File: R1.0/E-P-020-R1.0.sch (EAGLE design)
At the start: 42 parts, among them CN1 1X4-CLEANBIG, J1 1445055-3, U2 ATMEGA328P_PDIP

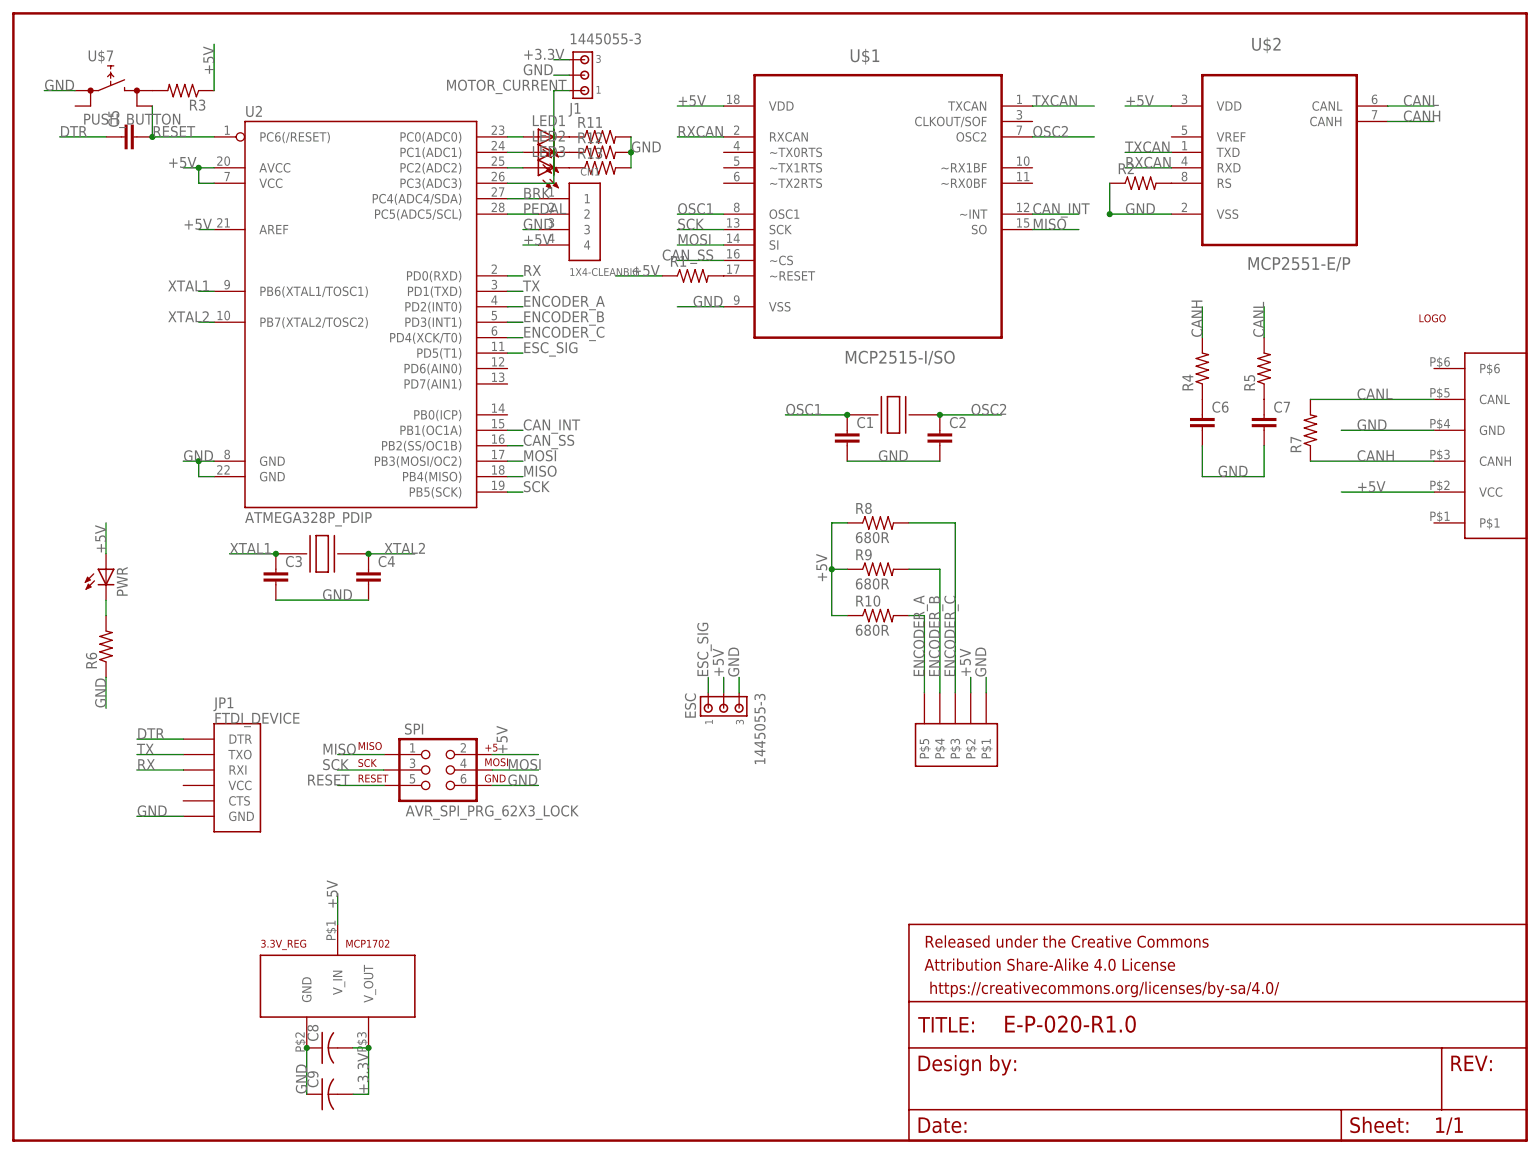
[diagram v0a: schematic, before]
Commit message: Added resistor/capacitor values
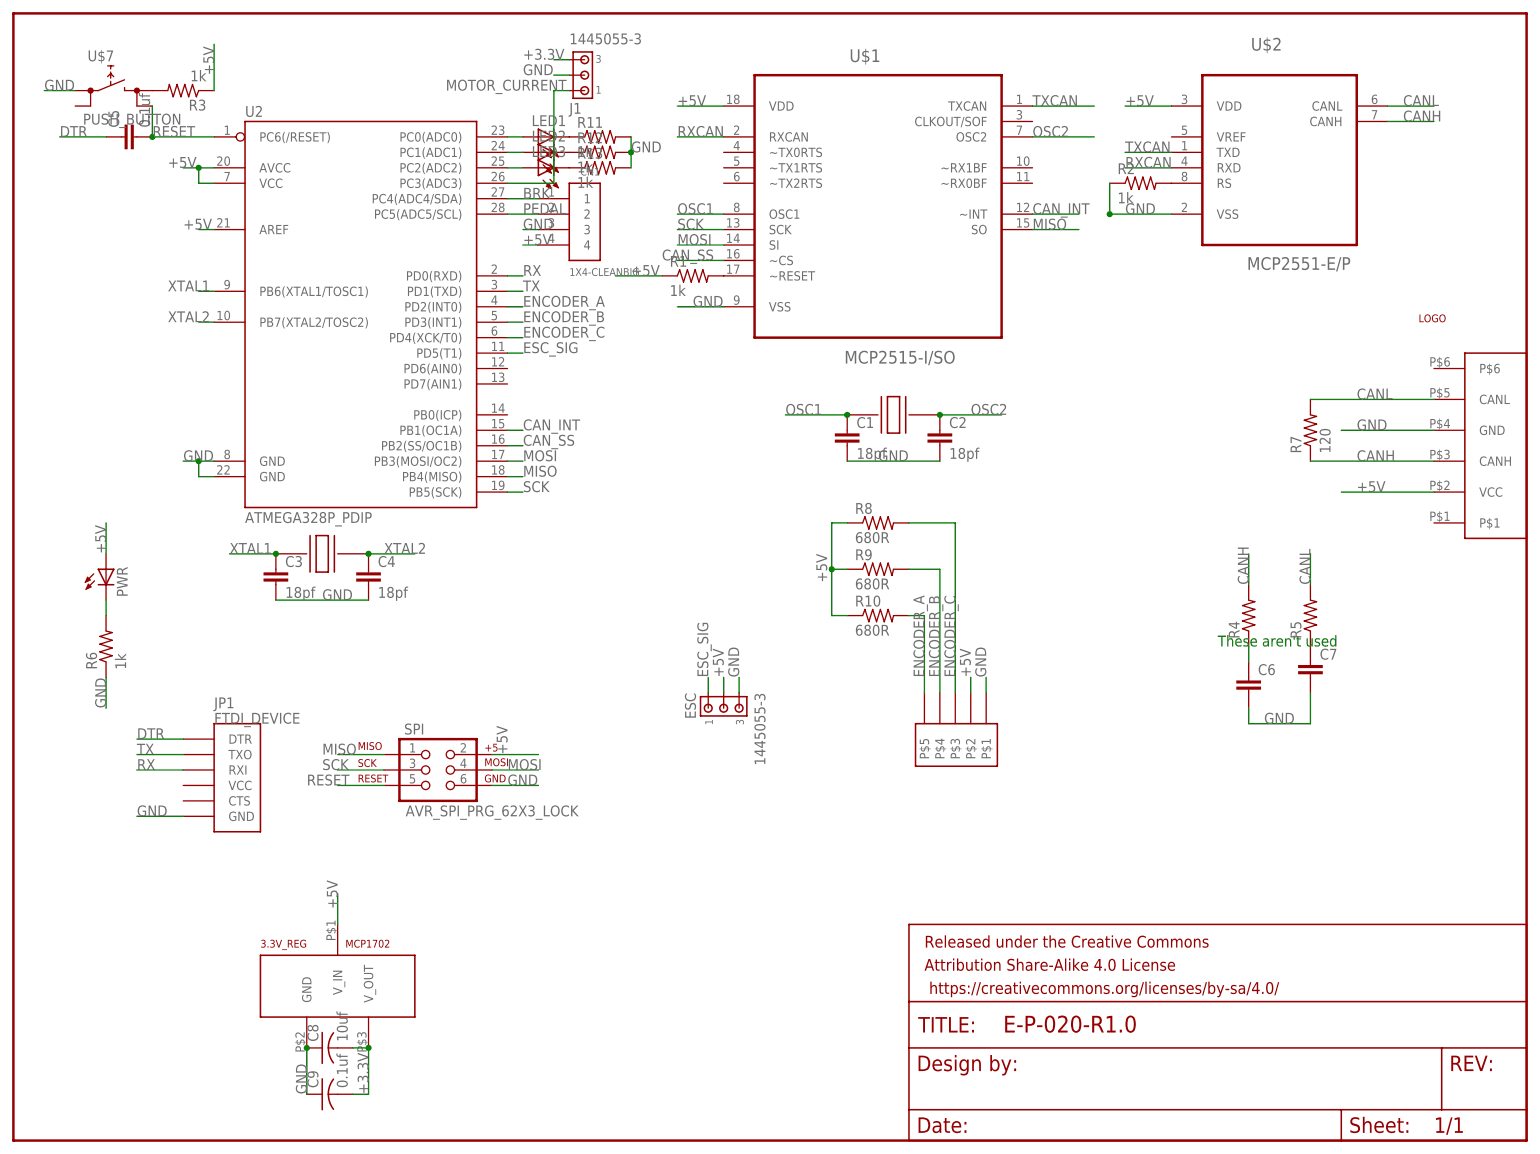
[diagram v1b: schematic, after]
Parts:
- C1, C2, C3, C4: value (none) -> 18pf
- C5, C9: value (none) -> 0.1uf
- C8: value (none) -> 10uf
- R1, R11, R12, R13, R2, R3, R6: value (none) -> 1k
- R7: value (none) -> 120
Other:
- note added: "These aren't used"
- moved on the sheet: C6, C7, R4, R5
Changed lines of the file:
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@@
 <part name="U$1" library="Microchip_By_element14_Batch_1" deviceset="MCP2515-I/SO" device=""/>
 <part name="U$2" library="Microchip_By_element14_Batch_1" deviceset="MCP2551-E/P" device=""/>
-<part name="R1" library="SparkFun-Passives" deviceset="RESISTOR" device="0805-RES"/>
+<part name="R1" library="SparkFun-Passives" deviceset="RESISTOR" device="0805-RES" value="1k"/>
 <part name="U$3" library="mylibrary" deviceset="CRYSTAL" device=""/>
-<part name="C1" library="SparkFun-Capacitors" deviceset="CAP" device="0805"/>
-<part name="C2" library="SparkFun-Capacitors" deviceset="CAP" device="0805"/>
+<part name="C1" library="SparkFun-Capacitors" deviceset="CAP" device="0805" value="18pf"/>
+<part name="C2" library="SparkFun-Capacitors" deviceset="CAP" device="0805" value="18pf"/>
 <part name="U$4" library="mylibrary" deviceset="CRYSTAL" device=""/>
-<part name="C3" library="SparkFun-Capacitors" deviceset="CAP" device="0805"/>
-<part name="C4" library="SparkFun-Capacitors" deviceset="CAP" device="0805"/>
-<part name="R2" library="SparkFun-Passives" deviceset="RESISTOR" device="0805-RES"/>
+<part name="C3" library="SparkFun-Capacitors" deviceset="CAP" device="0805" value="18pf"/>
+<part name="C4" library="SparkFun-Capacitors" deviceset="CAP" device="0805" value="18pf"/>
+<part name="R2" library="SparkFun-Passives" deviceset="RESISTOR" device="0805-RES" value="1k"/>
 <part name="JP1" library="SparkFun-Connectors" deviceset="FTDI_DEVICE" device=""/>
 <part name="SPI" library="SparkFun-Connectors" deviceset="AVR_SPI_PRG_6" device="2X3_LOCK"/>
 <part name="U$7" library="E-P-099-R2.2" deviceset="PUSH_BUTTON" device=""/>
-<part name="C5" library="SparkFun-Capacitors" deviceset="CAP" device="0805"/>
-<part name="R3" library="SparkFun-Passives" deviceset="RESISTOR" device="0805-RES"/>
+<part name="C5" library="SparkFun-Capacitors" deviceset="CAP" device="0805" value="0.1uf"/>
+<part name="R3" library="SparkFun-Passives" deviceset="RESISTOR" device="0805-RES" value="1k"/>
 <part name="R4" library="SparkFun-Passives" deviceset="RESISTOR" device="0805-RES"/>
 <part name="R5" library="SparkFun-Passives" deviceset="RESISTOR" device="0805-RES"/>
@@
 <part name="C7" library="SparkFun-Capacitors" deviceset="CAP" device="0805"/>
 <part name="PWR" library="E-P-099-R2.2" deviceset="LED" device="CHIPLED_1206"/>
-<part name="R6" library="SparkFun-Passives" deviceset="RESISTOR" device="0805-RES"/>
+<part name="R6" library="SparkFun-Passives" deviceset="RESISTOR" device="0805-RES" value="1k"/>
 <part name="U2" library="SparkFun-DigitalIC" deviceset="ATMEGA328P_PDIP" device=""/>
-<part name="R7" library="adafruit" deviceset="R-US_" device="M1206"/>
+<part name="R7" library="adafruit" deviceset="R-US_" device="M1206" value="120"/>
 <part name="R8" library="SparkFun-Resistors" deviceset="0.75OHM-1/4W-1%(0805)" device="" value="680R"/>
 <part name="R9" library="SparkFun-Resistors" deviceset="0.75OHM-1/4W-1%(0805)" device="" value="680R"/>
@@
 <part name="J1" library="con-amp" deviceset="1445055-3" device=""/>
 <part name="3.3V_REG" library="mylibrary" deviceset="MCP1702" device=""/>
-<part name="C8" library="adafruit" deviceset="C-US" device="C0805"/>
-<part name="C9" library="adafruit" deviceset="C-US" device="C0805"/>
+<part name="C8" library="adafruit" deviceset="C-US" device="C0805" value="10uf"/>
+<part name="C9" library="adafruit" deviceset="C-US" device="C0805" value="0.1uf"/>
 <part name="LED1" library="adafruit" deviceset="LED" device="SMT1206"/>
 <part name="LED2" library="adafruit" deviceset="LED" device="SMT1206"/>
 <part name="LED3" library="adafruit" deviceset="LED" device="SMT1206"/>
-<part name="R11" library="E-P-099-R2.2" deviceset="RESISTOR" device="0805-RES"/>
-<part name="R12" library="E-P-099-R2.2" deviceset="RESISTOR" device="0805-RES"/>
-<part name="R13" library="E-P-099-R2.2" deviceset="RESISTOR" device="0805-RES"/>
+<part name="R11" library="E-P-099-R2.2" deviceset="RESISTOR" device="0805-RES" value="1k"/>
+<part name="R12" library="E-P-099-R2.2" deviceset="RESISTOR" device="0805-RES" value="1k"/>
+<part name="R13" library="E-P-099-R2.2" deviceset="RESISTOR" device="0805-RES" value="1k"/>
 </parts>
 <sheets>
 <sheet>
 <plain>
+<text x="182.88" y="66.04" size="1.778" layer="91">These aren't used</text>
 </plain>
 <instances>
@@
 <instance part="C5" gate="G$1" x="5.08" y="149.86" rot="R90"/>
 <instance part="R3" gate="G$1" x="12.7" y="157.48" rot="R180"/>
-<instance part="R4" gate="G$1" x="180.34" y="111.76" rot="R90"/>
-<instance part="R5" gate="G$1" x="190.5" y="111.76" rot="R90"/>
-<instance part="C6" gate="G$1" x="180.34" y="101.6"/>
-<instance part="C7" gate="G$1" x="190.5" y="101.6"/>
+<instance part="R4" gate="G$1" x="187.96" y="71.12" rot="R90"/>
+<instance part="R5" gate="G$1" x="198.12" y="71.12" rot="R90"/>
+<instance part="C6" gate="G$1" x="187.96" y="58.42"/>
+<instance part="C7" gate="G$1" x="198.12" y="60.96"/>
 <instance part="PWR" gate="G$1" x="0" y="78.74"/>
 <instance part="R6" gate="G$1" x="0" y="66.04" rot="R90"/>
@@
 <segment>
 <pinref part="C6" gate="G$1" pin="2"/>
-<wire x1="180.34" y1="99.06" x2="180.34" y2="93.98" width="0.1524" layer="91"/>
+<wire x1="187.96" y1="55.88" x2="187.96" y2="53.34" width="0.1524" layer="91"/>
 <pinref part="C7" gate="G$1" pin="2"/>
-<wire x1="180.34" y1="93.98" x2="190.5" y2="93.98" width="0.1524" layer="91"/>
-<wire x1="190.5" y1="93.98" x2="190.5" y2="99.06" width="0.1524" layer="91"/>
-<label x="182.88" y="93.98" size="1.778" layer="95"/>
+<wire x1="187.96" y1="53.34" x2="198.12" y2="53.34" width="0.1524" layer="91"/>
+<wire x1="198.12" y1="53.34" x2="198.12" y2="58.42" width="0.1524" layer="91"/>
+<label x="190.5" y="53.34" size="1.778" layer="95"/>
 </segment>
 <segment>
@@
 <segment>
 <pinref part="R5" gate="G$1" pin="2"/>
-<wire x1="190.5" y1="116.84" x2="190.5" y2="121.92" width="0.1524" layer="91"/>
-<label x="190.5" y="116.84" size="1.778" layer="95" rot="R90"/>
+<wire x1="198.12" y1="76.2" x2="198.12" y2="81.28" width="0.1524" layer="91"/>
+<label x="198.12" y="76.2" size="1.778" layer="95" rot="R90"/>
 </segment>
 </net>
@@
 <segment>
 <pinref part="R4" gate="G$1" pin="2"/>
-<wire x1="180.34" y1="116.84" x2="180.34" y2="121.92" width="0.1524" layer="91"/>
-<label x="180.34" y="116.84" size="1.778" layer="95" rot="R90"/>
+<wire x1="187.96" y1="76.2" x2="187.96" y2="81.28" width="0.1524" layer="91"/>
+<label x="187.96" y="76.2" size="1.778" layer="95" rot="R90"/>
 </segment>
 </net>
@@
 <pinref part="R4" gate="G$1" pin="1"/>
 <pinref part="C6" gate="G$1" pin="1"/>
-</segment>
-</net>
+<wire x1="187.96" y1="63.5" x2="187.96" y2="66.04" width="0.1524" layer="91"/>
+</segment>
+</net>

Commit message: Integrated pedal, started working on the current sensor
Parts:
- R3: value 1k -> 10k
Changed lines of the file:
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@@
 <?xml version="1.0" encoding="utf-8"?>
 <!DOCTYPE eagle SYSTEM "eagle.dtd">
-<eagle version="7.5.0">
+<eagle version="7.2.0">
 <drawing>
 <settings>
@@
 <part name="U$7" library="E-P-099-R2.2" deviceset="PUSH_BUTTON" device=""/>
 <part name="C5" library="SparkFun-Capacitors" deviceset="CAP" device="0805" value="0.1uf"/>
-<part name="R3" library="SparkFun-Passives" deviceset="RESISTOR" device="0805-RES" value="1k"/>
+<part name="R3" library="SparkFun-Passives" deviceset="RESISTOR" device="0805-RES" value="10k"/>
 <part name="R4" library="SparkFun-Passives" deviceset="RESISTOR" device="0805-RES"/>
 <part name="R5" library="SparkFun-Passives" deviceset="RESISTOR" device="0805-RES"/>
